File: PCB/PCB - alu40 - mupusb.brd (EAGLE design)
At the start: 228 x 76 mm, 159 parts, among them IC1 XB3303ASOT23, IC2 TP4054-42-SOT25-R, J1 SK-3296S-01-L1, Q2 PMOSFET, Q3 PMOSFET, Q5 PMOSFET, Q6 NMOSFET, U1 ISP1807-LRISP1807-LR_ISP1807-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, X1 BM02B-SRSS-TB

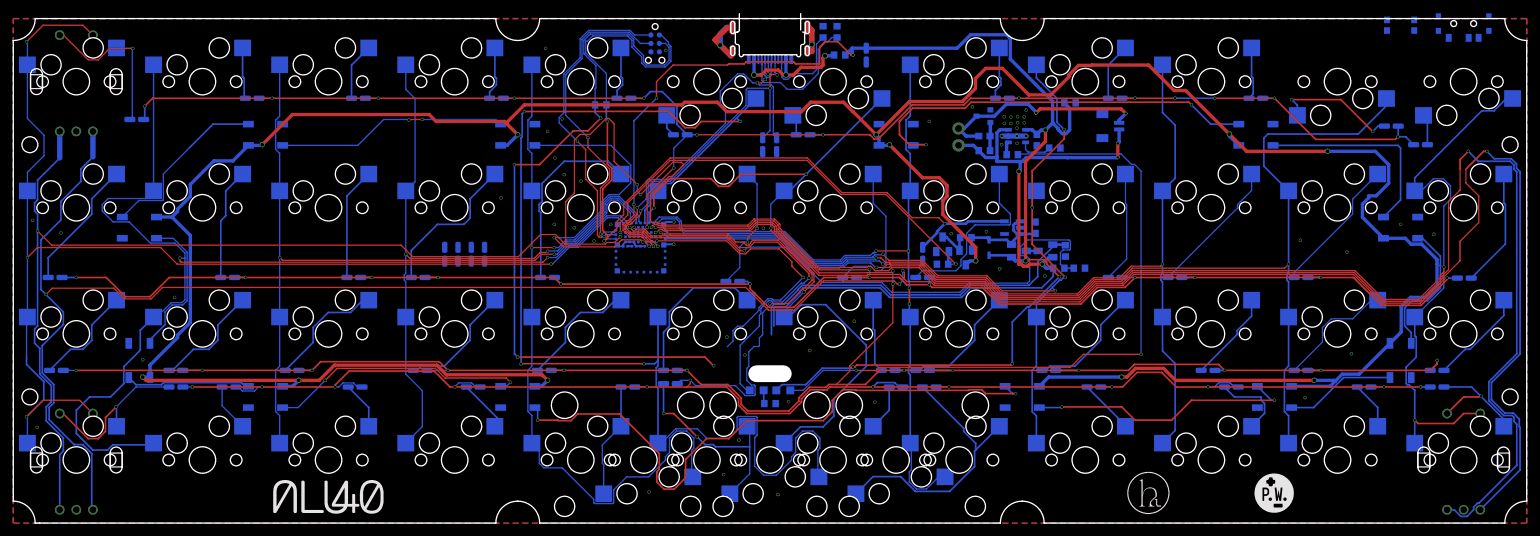
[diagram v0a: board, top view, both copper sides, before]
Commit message: Route new switch footprints
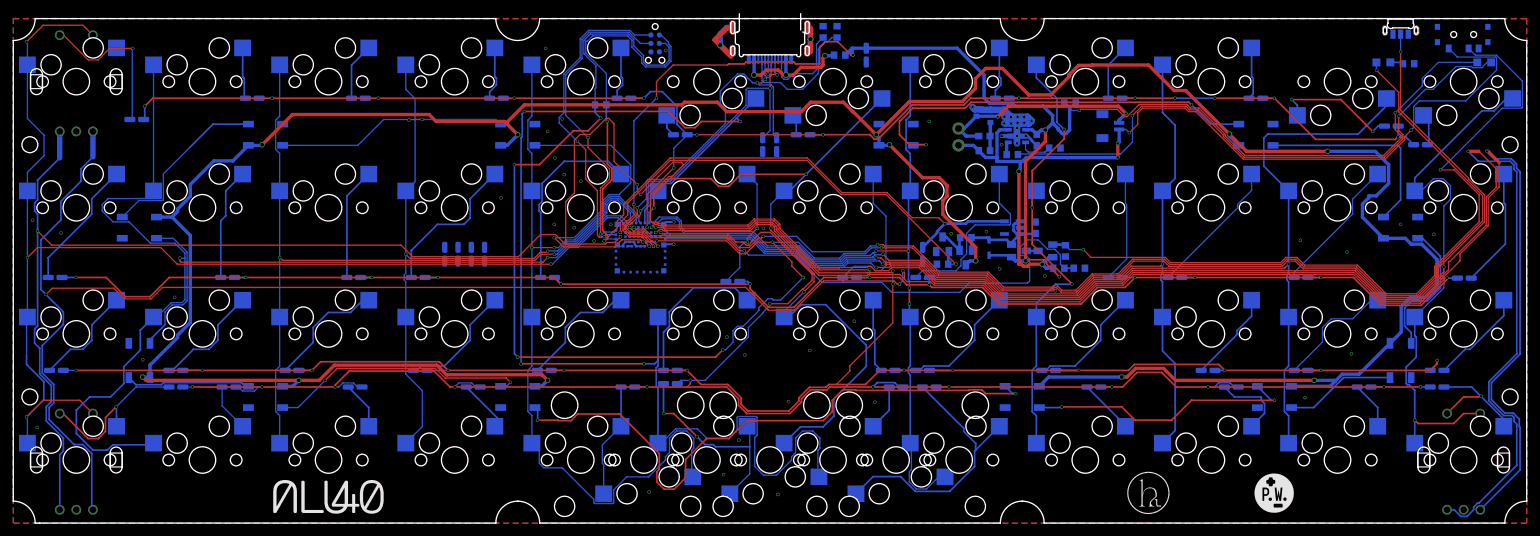
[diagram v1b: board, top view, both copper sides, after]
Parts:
- removed S5: MOMENTARY-SWITCH-SPST-SMD-4.6X2.8MM, Volume_V1:TACTILE_SWITCH_SMD_4.6X2.8MM
- added S1: PTS847MM160LSMTR2_LFS, PTS847MM160LSMTR2_LFS:SW_PTS847MM160LSMTR2_LFS
- moved LED2 116.6 mm to (221.6, 69.4)
- moved R1 109.0 mm to (210.2, 69.2)
- moved LED1 106.5 mm to (206.4, 69.4)
- moved J1 0.40 mm to (218.5, 73.6)
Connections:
- net GND: now also S1.1, S1.3, S1.S1, S1.S2; no longer S5.1, S5.2
- net RESET: now also S1.2; no longer S5.3, S5.4
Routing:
- net RESET: track 152.3 -> 311.1 mm, vias 6 -> 9
- net BLED: track 54.4 -> 175.1 mm, vias 2 -> 4
- net N$75: track 55.1 -> 115.1 mm, vias 0 -> 2
- net V_BATT: track 108.1 -> 138.9 mm, vias 4 -> 6
- net V_USB: track 206.9 -> 226.8 mm
- net GND: track 36.0 -> 55.7 mm, vias 58 -> 59
- net N$60: track 102.4 -> 88.9 mm
- net ROW3: track 292.4 -> 284.1 mm
- net A: track 432.4 -> 436.9 mm
- net BVOLT: track 86.6 -> 82.2 mm
- net COL8: track 135.1 -> 137.1 mm
- net N$12: track 4.04 -> 5.27 mm
- net COL10: track 169.5 -> 170.6 mm
- net G_BAT: track 33.2 -> 32.7 mm
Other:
- outline, holes or cut-outs redrawn

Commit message: Commit gerbers
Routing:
- net N$85: track 93.4 -> 82.6 mm
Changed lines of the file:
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@@
 <wire x1="110.95" y1="14.18" x2="110.95" y2="11.5" width="0.2032" layer="16"/>
 <wire x1="110.95" y1="11.5" x2="110.95" y2="7.42" width="0.2032" layer="16"/>
-<via x="103.005421875" y="13.005421875" extent="1-16" drill="0.35"/>
+<via x="104.205421875" y="13.405421875" extent="1-16" drill="0.35"/>
 <wire x1="110.95" y1="11.5" x2="105.786775" y2="11.5" width="0.254" layer="16"/>
-<wire x1="105.786775" y1="11.5" x2="105.462675" y2="11.8241" width="0.254" layer="16"/>
-<wire x1="105.462675" y1="11.8241" x2="104.18674375" y2="11.8241" width="0.254" layer="16"/>
-<wire x1="104.18674375" y1="11.8241" x2="103.005421875" y2="13.005421875" width="0.254" layer="16"/>
-<wire x1="103.005421875" y1="13.005421875" x2="99.51084375" y2="16.5" width="0.254" layer="1"/>
-<wire x1="99.51084375" y1="16.5" x2="98" y2="16.5" width="0.254" layer="1"/>
+<wire x1="104.205421875" y1="13.405421875" x2="104.205421875" y2="13.08135625" width="0.254" layer="16"/>
+<wire x1="105.786775" y1="11.5" x2="104.205421875" y2="13.08135625" width="0.254" layer="16"/>
+<wire x1="104.205421875" y1="13.405421875" x2="102.71084375" y2="14.9" width="0.254" layer="1"/>
+<wire x1="102.71084375" y1="14.9" x2="99.6" y2="14.9" width="0.254" layer="1"/>
+<wire x1="99.6" y1="14.9" x2="98" y2="16.5" width="0.254" layer="1"/>
 <via x="98" y="16.5" extent="1-16" drill="0.35"/>
 <wire x1="98" y1="16.5" x2="97.96" y2="16.54" width="0.254" layer="16"/>
@@
 <wire x1="111.7013" y1="8.54784375" x2="111.7013" y2="12.8830125" width="0.2032" layer="16"/>
 <wire x1="111.7013" y1="12.8830125" x2="112.0536" y2="13.2353125" width="0.2032" layer="16"/>
-<wire x1="97.63670625" y1="12.04" x2="97.13" y2="12.04" width="0.2032" layer="16"/>
-<wire x1="99.79570625" y1="14.199" x2="97.63670625" y2="12.04" width="0.2032" layer="16"/>
+<wire x1="97.13" y1="12.04" x2="97.13" y2="12.13329375" width="0.2032" layer="16"/>
+<wire x1="99.19570625" y1="14.199" x2="97.13" y2="12.13329375" width="0.2032" layer="16"/>
 <wire x1="121.37" y1="6.96" x2="121.2013" y2="7.1287" width="0.2032" layer="16"/>
 <wire x1="121.2013" y1="7.1287" x2="121.2013" y2="10.96498125" width="0.2032" layer="16"/>
 <wire x1="121.2013" y1="10.96498125" x2="121.5188" y2="11.28248125" width="0.2032" layer="16"/>
 <wire x1="109.0464" y1="15.9246875" x2="109.0464" y2="14.00008125" width="0.2032" layer="16"/>
-<wire x1="103.05185625" y1="14.199" x2="99.79570625" y2="14.199" width="0.2032" layer="16"/>
+<wire x1="104.65185625" y1="14.199" x2="99.19570625" y2="14.199" width="0.2032" layer="16"/>
 <wire x1="109.0464" y1="14.00008125" x2="107.79751875" y2="12.7512" width="0.2032" layer="16"/>
-<wire x1="107.79751875" y1="12.7512" x2="104.49965625" y2="12.7512" width="0.2032" layer="16"/>
-<wire x1="104.49965625" y1="12.7512" x2="103.05185625" y2="14.199" width="0.2032" layer="16"/>
+<wire x1="107.79751875" y1="12.7512" x2="106.09965625" y2="12.7512" width="0.2032" layer="16"/>
+<wire x1="106.09965625" y1="12.7512" x2="104.65185625" y2="14.199" width="0.2032" layer="16"/>
 <contactref element="U1" pad="42"/>
 <wire x1="97.13" y1="12.04" x2="97.13" y2="20.34521875" width="0.254" layer="16"/>
@@
 <wire x1="126.900675" y1="20.0791" x2="124.975325" y2="20.0791" width="0.254" layer="1"/>
 <wire x1="123.3861" y1="16.792325" x2="122.024675" y2="15.4309" width="0.254" layer="1"/>
-<wire x1="99.5780375" y1="5.1058" x2="98.0419625" y2="5.1058" width="0.254" layer="1"/>
-<wire x1="98.0419625" y1="5.1058" x2="96.9558" y2="6.1919625" width="0.254" layer="1"/>
-<wire x1="96.9558" y1="6.1919625" x2="96.9558" y2="7.7280375" width="0.254" layer="1"/>
 <wire x1="84.024675" y1="15.4309" x2="82.099325" y2="15.4309" width="0.254" layer="1"/>
 <wire x1="123.3861" y1="18.489875" x2="123.3861" y2="16.792325" width="0.254" layer="1"/>
@@
 <wire x1="126.996275" y1="19.9835" x2="126.900675" y2="20.0791" width="0.254" layer="1"/>
 <wire x1="85.027975" y1="16.4342" x2="84.024675" y2="15.4309" width="0.254" layer="1"/>
-<wire x1="101.2865" y1="6.8142625" x2="99.5780375" y2="5.1058" width="0.254" layer="1"/>
-<wire x1="91.352575" y1="16.4342" x2="85.027975" y2="16.4342" width="0.254" layer="1"/>
-<wire x1="96.9558" y1="7.7280375" x2="97.3241" y2="8.0963375" width="0.254" layer="1"/>
-<wire x1="97.3241" y1="8.0963375" x2="97.3241" y2="10.462675" width="0.254" layer="1"/>
-<wire x1="97.3241" y1="10.462675" x2="91.352575" y2="16.4342" width="0.254" layer="1"/>
+<wire x1="91.548059375" y1="16.4342" x2="85.027975" y2="16.4342" width="0.254" layer="1"/>
+<wire x1="94.088059375" y1="13.8942" x2="91.548059375" y2="16.4342" width="0.254" layer="1"/>
 <wire x1="122.024675" y1="15.4309" x2="110.5131375" y2="15.4309" width="0.254" layer="1"/>
-<wire x1="110.5131375" y1="15.4309" x2="107.8080375" y2="12.7258" width="0.254" layer="1"/>
-<wire x1="107.8080375" y1="12.7258" x2="104.439025" y2="12.7258" width="0.254" layer="1"/>
-<wire x1="104.439025" y1="12.7258" x2="101.2865" y2="9.573275" width="0.254" layer="1"/>
-<wire x1="101.2865" y1="9.573275" x2="101.2865" y2="6.8142625" width="0.254" layer="1"/>
+<wire x1="107.6080375" y1="12.5258" x2="110.5131375" y2="15.4309" width="0.254" layer="1"/>
 <wire x1="79" y1="15.5" x2="79" y2="16.977" width="0.254" layer="16"/>
 <wire x1="79" y1="16.977" x2="78.577" y2="17.4" width="0.254" layer="16"/>
+<wire x1="101.4580375" y1="13.8942" x2="102.8264375" y2="12.5258" width="0.254" layer="1"/>
+<wire x1="94.088059375" y1="13.8942" x2="101.4580375" y2="13.8942" width="0.254" layer="1"/>
+<wire x1="102.8264375" y1="12.5258" x2="107.6080375" y2="12.5258" width="0.254" layer="1"/>
 </signal>
 <signal name="N$86">
